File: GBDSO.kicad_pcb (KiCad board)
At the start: 2 copper layers, 51 x 61 mm, 73 parts, among them J1 MJ-3523-SMT-TR, J2 MJ-3523-SMT-TR, J3 Conn_01x32, P1 100k, P2 100k, SW1 SW_SPDT, SW2 SW_SPDT, U1 TL062, U2 DS1267_SOIC, U3 TL062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

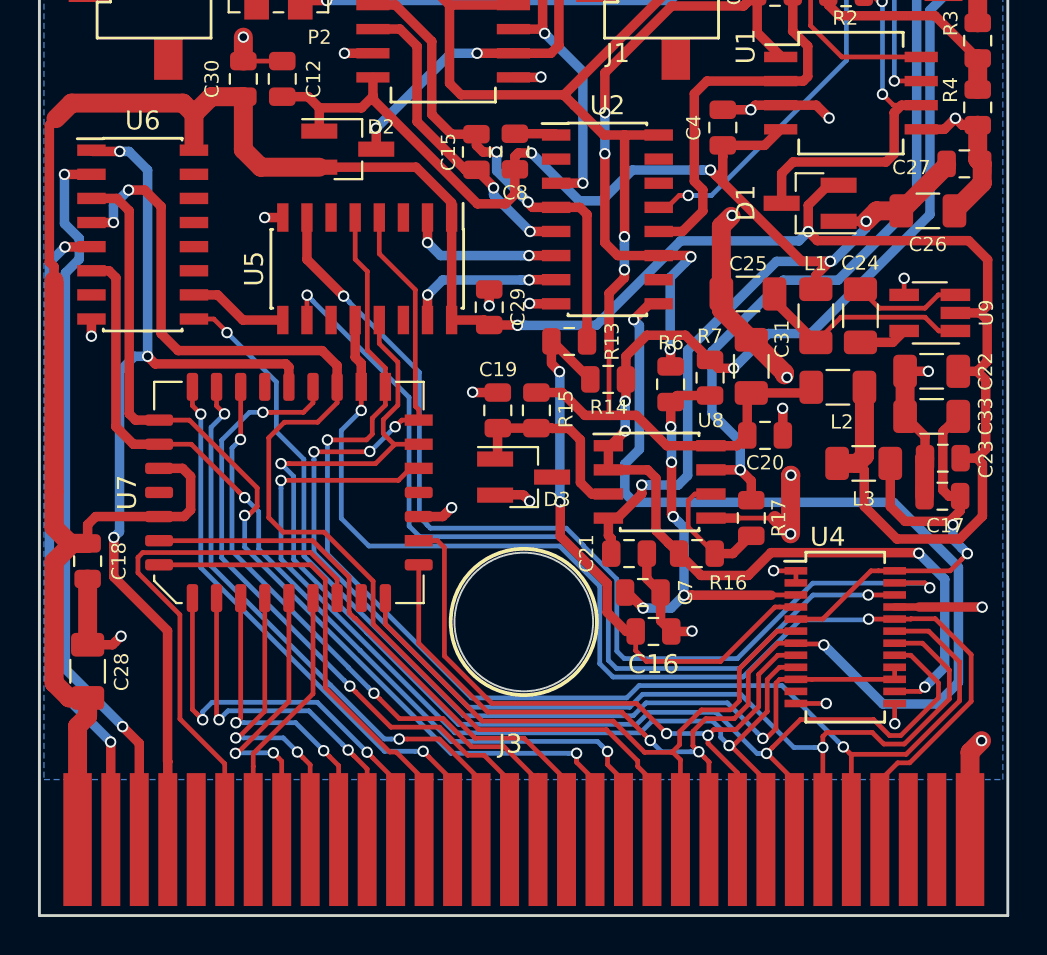
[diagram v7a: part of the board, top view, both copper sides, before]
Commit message: added jumpers to the schematic and pcb so that the EPROM can be programmed on the cartridge
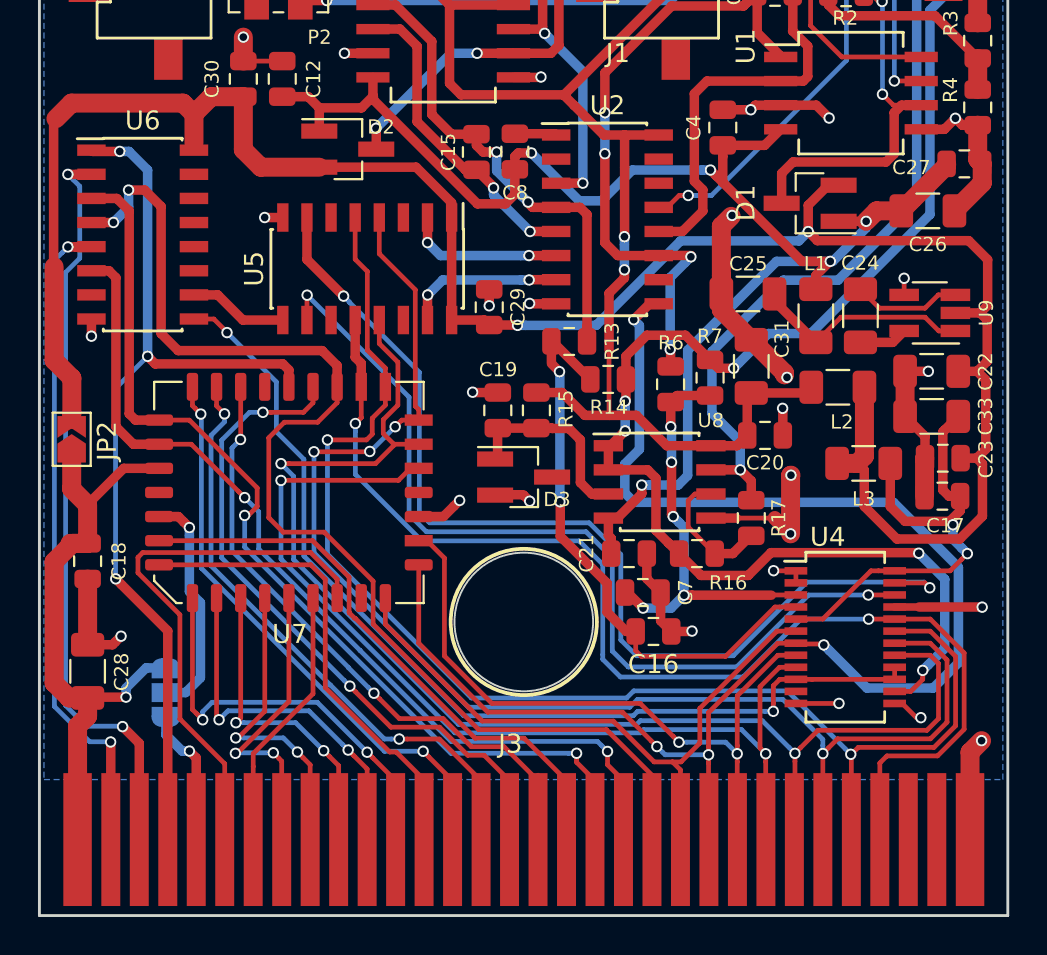
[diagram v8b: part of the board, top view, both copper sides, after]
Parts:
- added JP1: SolderJumper_3_Open, Jumper:SolderJumper-3_P1.3mm_Open_RoundedPad1.0x1.5mm_NumberLabels, B.Cu at (87.4, 140.4)
- added JP2: SolderJumper_2_Open, Jumper:SolderJumper-2_P1.3mm_Open_TrianglePad1.0x1.5mm, F.Cu at (82.5, 127.1)
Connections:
- J3 pad 5: Net-(J3-Pad5) -> /VPP
- U7 pad 2: +5V -> Net-(JP1-Pad2)
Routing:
- net Net-(JP1-Pad2): track 0.00 -> 12.1 mm, vias 0 -> 1
- net /VPP: track 0.00 -> 7.33 mm, vias 0 -> 1
- net /D1: track 82.4 -> 80.1 mm
- net Net-(U4-Pad10): track 54.5 -> 52.3 mm
- net GND: track 102.6 -> 104.5 mm
- net /D7: track 64.1 -> 62.9 mm
- net /~WR: track 38.6 -> 39.5 mm
- net /~RD: track 49.6 -> 49.0 mm
- net +5V: track 154.9 -> 155.4 mm, vias 2 -> 3
